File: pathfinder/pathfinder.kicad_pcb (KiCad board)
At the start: 4 copper layers, 30 x 8.1 mm, 66 parts, among them IC1 TESEO-LIV3R, IC2 BMI323, IC3 BMP390, IC4 BGA725L6E6327FTSA1, IC5 ST730M33R, J3 CAS left, J4 CAS right, P2 USB_C_Plug_USB2.0, U1 STM32F042C6Ux, U2 LP2985-1.8, U3 ECMF02-2AMX6, U4 B39162B4327P810

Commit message: Start components layout
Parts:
- removed D6: Green, Diode_SMD:D_0603_1608Metric_Pad1.05x0.95mm_HandSolder
- removed R6: 420, Resistor_SMD:R_0603_1608Metric_Pad0.98x0.95mm_HandSolder
- AC1: footprint sensor_fuser:LGA-12 -> pathfinder:LGA-12
- C1, C10, C11, C12, C13, C14, C15, C16, C17, C18, C19, C2, C20, C21, C22, C23, C24, C25, C26, C27, C28, C3, C4, C5, C6, C7, C8, C9: footprint Capacitor_SMD:C_0603_1608Metric_Pad1.08x0.95mm_HandSolder -> Capacitor_SMD:C_0402_1005Metric_Pad0.74x0.62mm_HandSolder
- D1, D2, D4, D5, D8: footprint Diode_SMD:D_0603_1608Metric_Pad1.05x0.95mm_HandSolder -> Diode_SMD:D_0402_1005Metric_Pad0.77x0.64mm_HandSolder
- R1, R10, R2, R3, R4, R5, R7, R8, R9: footprint Resistor_SMD:R_0603_1608Metric_Pad0.98x0.95mm_HandSolder -> Resistor_SMD:R_0402_1005Metric_Pad0.72x0.64mm_HandSolder
- moved R7 159.8 mm to (131.8, 51.3), turned to -90 degrees
- moved R5 156.8 mm to (130.1, 51.3), turned to -90 degrees
- moved C16 153.0 mm to (146.3, 67.4), turned to -90 degrees
- moved R8 152.7 mm to (136.7, 67.8), turned to 180 degrees
- moved C17 151.3 mm to (141.7, 67.3), turned to -90 degrees
- moved D5 149.3 mm to (131.8, 49.0), turned to -90 degrees
- moved C15 146.9 mm to (143.4, 70.9)
- moved U2 146.3 mm to (144.0, 68.3)
- moved D4 146.3 mm to (130.1, 49.0), turned to -90 degrees
- moved D8 143.5 mm to (136.7, 66.7)
- moved IC5 142.4 mm to (133.8, 68.3)
- moved D7 139.2 mm to (130.9, 64.4), turned to 90 degrees
- moved C11 138.7 mm to (130.9, 66.7), turned to 180 degrees
- moved C10 136.3 mm to (130.9, 67.8), turned to 180 degrees
- moved C9 133.9 mm to (130.9, 68.8), turned to 180 degrees
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
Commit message: Board finished
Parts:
- removed D4: Green, Diode_SMD:D_0402_1005Metric_Pad0.77x0.64mm_HandSolder
- removed P2: USB_C_Plug_USB2.0, Connector_USB:USB_C_Receptacle_G-Switch_GT-USB-7010ASV
- added C29: 100n, Capacitor_SMD:C_0402_1005Metric_Pad0.74x0.62mm_HandSolder, F.Cu at (132.3, 86.9)
- added C30: 100n, Capacitor_SMD:C_0402_1005Metric_Pad0.74x0.62mm_HandSolder, F.Cu at (129.8, 89.1)
- added C31: 23p, Capacitor_SMD:C_0402_1005Metric_Pad0.74x0.62mm_HandSolder, F.Cu at (134.9, 84.1)
- added C32: 23p, Capacitor_SMD:C_0402_1005Metric_Pad0.74x0.62mm_HandSolder, F.Cu at (135.6, 87.8)
- added D6: SZNUP2105L, Package_TO_SOT_SMD:SOT-23, F.Cu at (130.0, 82.6)
- added IC6: TCAN3413DDFR, pathfinder:SOT65P280X110-8N, F.Cu at (130.0, 86.5)
- added J1: USB_C_Receptacle_USB2.0_14P, Connector_USB:USB_C_Receptacle_GCT_USB4105-xx-A_16P_TopMnt_Horizontal, F.Cu at (139.2, 58.3)
- added J2: RF IN, pathfinder:CONUFL001SMDT, F.Cu at (150.2, 101.5)
- added JP1: CAN jumper, Jumper:SolderJumper-2_P1.3mm_Open_RoundedPad1.0x1.5mm, F.Cu at (126.2, 89.3)
- added R11: 3.3k, Resistor_SMD:R_0402_1005Metric_Pad0.72x0.64mm_HandSolder, F.Cu at (148.2, 83.1)
- added R6: 120, Resistor_SMD:R_0402_1005Metric_Pad0.72x0.64mm_HandSolder, F.Cu at (126.2, 87.0)
- added Y1: 16Mhz, Crystal:Crystal_SMD_2016-4Pin_2.0x1.6mm, F.Cu at (135.3, 86.0)
- U1: value STM32F042C6Ux -> STM32G431CBUx
- moved R3 83.2 mm to (150.4, 89.1), turned to 180 degrees
- moved R4 82.7 mm to (150.4, 92.2), turned to 180 degrees
- moved D2 76.6 mm to (150.4, 91.2)
- moved D1 75.2 mm to (150.4, 90.2)
- moved C24 70.8 mm to (128.1, 98.0), turned to 180 degrees
- moved C23 67.4 mm to (142.7, 100.8), turned to 90 degrees
- moved C28 66.2 mm to (150.2, 105.5), turned to -90 degrees
- moved R10 66.1 mm to (142.7, 103.1), turned to -90 degrees
- moved C25 62.3 mm to (128.1, 99.1), turned to 180 degrees
- moved C22 61.5 mm to (128.1, 102.4)
- moved C27 60.9 mm to (146.7, 107.5)
- moved R9 60.8 mm to (128.1, 105.9)
- moved C26 59.6 mm to (142.7, 105.4), turned to 90 degrees
- moved L3 59.3 mm to (148.9, 106.0), turned to 90 degrees
- moved L2 58.2 mm to (127.5, 103.6), turned to 180 degrees
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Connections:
- AC1 pad 1: /Magnetometer/SCL -> /I2C1_SCL
- AC1 pad 11: /Magnetometer/ACC_INT1 -> /ACC2_INT1
- AC1 pad 12: /Magnetometer/ACC_INT2 -> /ACC2_INT2
- AC1 pad 4: /Magnetometer/SDA -> /I2C1_SDA
- AC1 pad 7: /Magnetometer/INT1 -> /MAG_INT1
- C10 pad 1: Net-(D3-K) -> /Power/PWR
- C11 pad 1: Net-(D3-K) -> /Power/PWR
- C15 pad 1: Net-(D3-K) -> /Power/PWR
- C24 pad 1: /GPS/UART_RX -> /UART1_RX
- C25 pad 1: /GPS/UART_TX -> /UART1_TX
- D3 pad 1: Net-(D3-K) -> /Power/PWR
- D7 pad 1: Net-(D3-K) -> /Power/PWR
- H4 pad 1: GND -> unconnected-(H4-Pad1)
- IC1 pad 2: /GPS/UART_RX -> /UART1_RX
- IC1 pad 3: /GPS/UART_TX -> /UART1_TX
- IC2 pad 1: /IMU/MISO -> /SPI1_MISO
- IC2 pad 12: /IMU/CSB -> /SPI1_CS
- IC2 pad 13: /IMU/SCK -> /SPI1_SCK
- IC2 pad 14: /IMU/MOSI -> /SPI1_MOSI
- IC2 pad 4: /IMU/INT1 -> /IMU_INT1
- IC2 pad 9: /IMU/INT2 -> /IMU_INT2
- IC3 pad 2: /Barometer/SCL -> /I2C1_SCL
- IC3 pad 4: /Barometer/SDA -> /I2C1_SDA
- IC3 pad 7: /Barometer/INT -> /BAR_INT1
- IC5 pad 3: Net-(D3-K) -> /Power/PWR
- IC5 pad 5: Net-(D3-K) -> /Power/PWR
- J3 pad 10: GND -> /CAN+
- J3 pad 3: unconnected-(J3-Pin_3-Pad3) -> +3V3
- J3 pad 4: unconnected-(J3-Pin_4-Pad4) -> GND
- J3 pad 5: unconnected-(J3-Pin_5-Pad5) -> /SPI1_MOSI
- J3 pad 6: unconnected-(J3-Pin_6-Pad6) -> /SPI1_MISO
- J3 pad 7: unconnected-(J3-Pin_7-Pad7) -> /SPI1_SCK
- J3 pad 8: unconnected-(J3-Pin_8-Pad8) -> /SPI1_CS
- J3 pad 9: unconnected-(J3-Pin_9-Pad9) -> /CAN-
- J4 pad 10: +3V3 -> /SWD
- J4 pad 3: unconnected-(J4-Pin_3-Pad3) -> /I2C1_SCL
- J4 pad 4: unconnected-(J4-Pin_4-Pad4) -> /I2C1_SDA
- J4 pad 5: unconnected-(J4-Pin_5-Pad5) -> /USART1_RX
- J4 pad 6: unconnected-(J4-Pin_6-Pad6) -> /USART1_TX
- J4 pad 7: unconnected-(J4-Pin_7-Pad7) -> GND
- J4 pad 8: unconnected-(J4-Pin_8-Pad8) -> /NRST
- J4 pad 9: unconnected-(J4-Pin_9-Pad9) -> /CLK
- R1 pad 2: /Barometer/SDA -> /I2C1_SDA
- R2 pad 2: /Barometer/SCL -> /I2C1_SCL
- R5 pad 1: Net-(D4-A) -> Net-(U1-PG10)
- R5 pad 2: Net-(D3-K) -> +3V3
- R7 pad 2: Net-(D3-K) -> /Power/PWR
- U1 pad 10: unconnected-(U1-PA0-Pad10) -> /UART1_TX
- U1 pad 11: unconnected-(U1-PA1-Pad11) -> /UART1_RX
- U1 pad 12: unconnected-(U1-PA2-Pad12) -> /SPI1_CS
- U1 pad 13: unconnected-(U1-PA3-Pad13) -> /SPI1_SCK
- U1 pad 14: unconnected-(U1-PA4-Pad14) -> /SPI1_MISO
- U1 pad 15: unconnected-(U1-PA5-Pad15) -> /SPI1_MOSI
- U1 pad 2: unconnected-(U1-PC13-Pad2) -> /IMU_INT1
- U1 pad 21: unconnected-(U1-PB10-Pad21) -> /MCU_PWR
- U1 pad 22: unconnected-(U1-PB11-Pad22) -> /USART1_TX
- U1 pad 23: GND -> /MCU_PWR
- U1 pad 24: /MCU_PWR -> /USART1_RX
- U1 pad 29: unconnected-(U1-PA8-Pad29) -> /ACC2_INT2
- U1 pad 3: unconnected-(U1-PC14-Pad3) -> /IMU_INT2
- U1 pad 30: unconnected-(U1-PA9-Pad30) -> /ACC2_INT1
- U1 pad 31: unconnected-(U1-PA10-Pad31) -> /DEBUG_LED1
- U1 pad 32: unconnected-(U1-PA11-Pad32) -> /DEBUG_LED0
- U1 pad 33: unconnected-(U1-PA12-Pad33) -> /USB_DM
- U1 pad 34: unconnected-(U1-PA13-Pad34) -> /USB_DP
- U1 pad 35: GND -> /MCU_PWR
- U1 pad 36: /MCU_PWR -> /SWD
- U1 pad 37: unconnected-(U1-PA14-Pad37) -> /CLK
- U1 pad 38: unconnected-(U1-PA15-Pad38) -> /I2C1_SCL
- U1 pad 39: unconnected-(U1-PB3-Pad39) -> /MAG_INT1
- U1 pad 41: unconnected-(U1-PB5-Pad41) -> /SWO
- U1 pad 44: unconnected-(U1-PF11-Pad44) -> /BAR_INT1
- U1 pad 45: unconnected-(U1-PB8-Pad45) -> /I2C1_SDA
- U1 pad 46: unconnected-(U1-PB9-Pad46) -> /FDCAN_RX
- U1 pad 47: GND -> /FDCAN_TX
- U1 pad 5: unconnected-(U1-PF0-Pad5) -> Net-(U1-PF0)
- U1 pad 6: unconnected-(U1-PF1-Pad6) -> Net-(U1-PF1)
- U1 pad 7: unconnected-(U1-NRST-Pad7) -> Net-(U1-PG10)
- U1 pad 8: GND -> unconnected-(U1-PA0-Pad8)
- U1 pad 9: /MCU_PWR -> unconnected-(U1-PA1-Pad9)
- U2 pad 1: Net-(D3-K) -> /Power/PWR
- U2 pad 3: Net-(D3-K) -> /Power/PWR
- U3 pad 5: /USB/D- -> /USB_DM
- U3 pad 6: /USB/D+ -> /USB_DP
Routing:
- net GND: track 0.00 -> 61.3 mm, vias 0 -> 254
- net /SPI1_CS: track 0.00 -> 43.7 mm, vias 0 -> 2
- net /SPI1_MOSI: track 0.00 -> 43.6 mm, vias 0 -> 2
- net /SPI1_SCK: track 0.00 -> 41.3 mm, vias 0 -> 2
- net /SPI1_MISO: track 0.00 -> 41.2 mm, vias 0 -> 2
- net /I2C1_SCL: track 0.00 -> 35.2 mm, vias 0 -> 4
- net /MCU_PWR: track 0.00 -> 33.2 mm, vias 0 -> 6
- net /USB_DP: track 0.00 -> 32.6 mm, vias 0 -> 2
- net /I2C1_SDA: track 0.00 -> 31.1 mm, vias 0 -> 4
- net /USB_DM: track 0.00 -> 30.7 mm
- net +3V3: track 0.00 -> 27.9 mm, vias 0 -> 17
- net /USART1_TX: track 0.00 -> 25.5 mm
- net +5V: track 0.00 -> 23.8 mm, vias 0 -> 2
- net /USART1_RX: track 0.00 -> 22.6 mm
- net /ACC2_INT2: track 0.00 -> 20.9 mm, vias 0 -> 2
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- added copper zone on In1.Cu, net +3V3
- added copper zone on F.Cu, net /Power/PWR
- added copper zone on B.Cu, net GND
- added copper zone on F.Cu, net GND
- added copper zone on F.Cu, net Net-(IC1-VBATT)
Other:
- board size 30 x 8.1 mm -> 30 x 57.8 mm

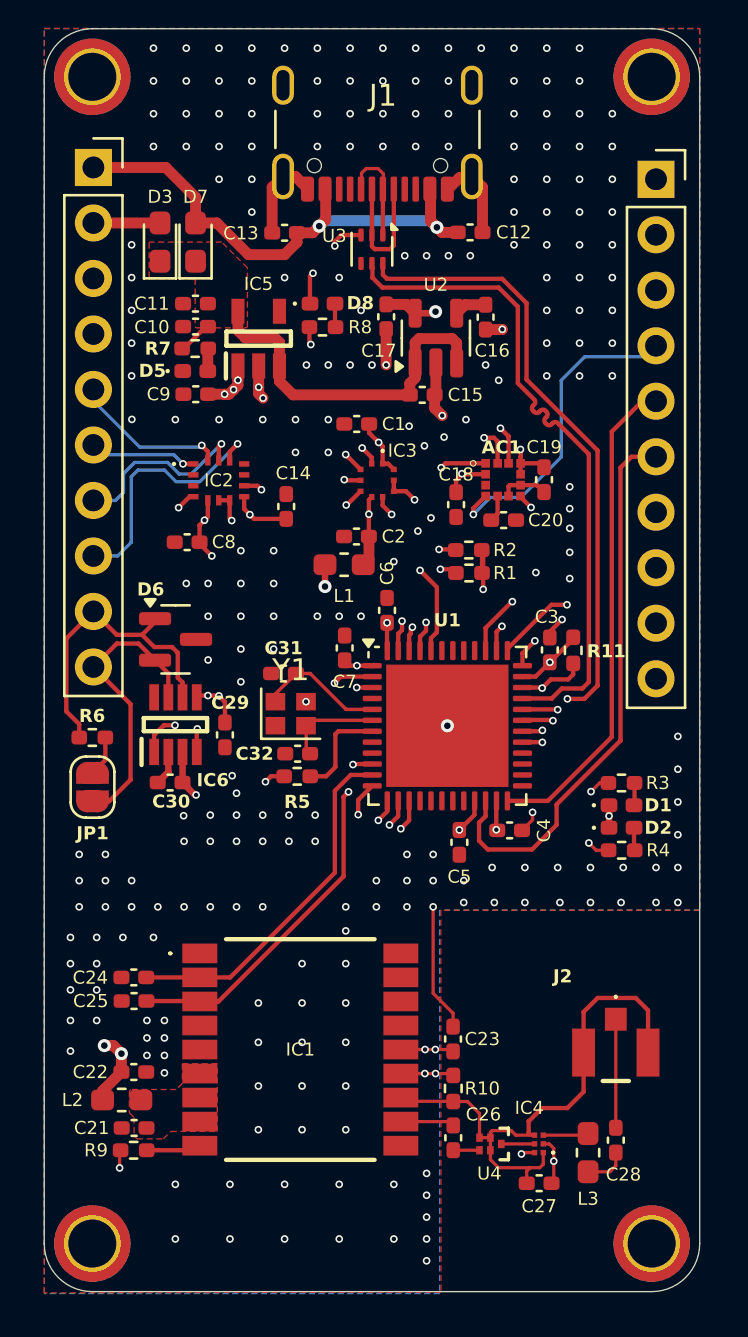
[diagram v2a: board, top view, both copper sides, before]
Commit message: Add optocoupler
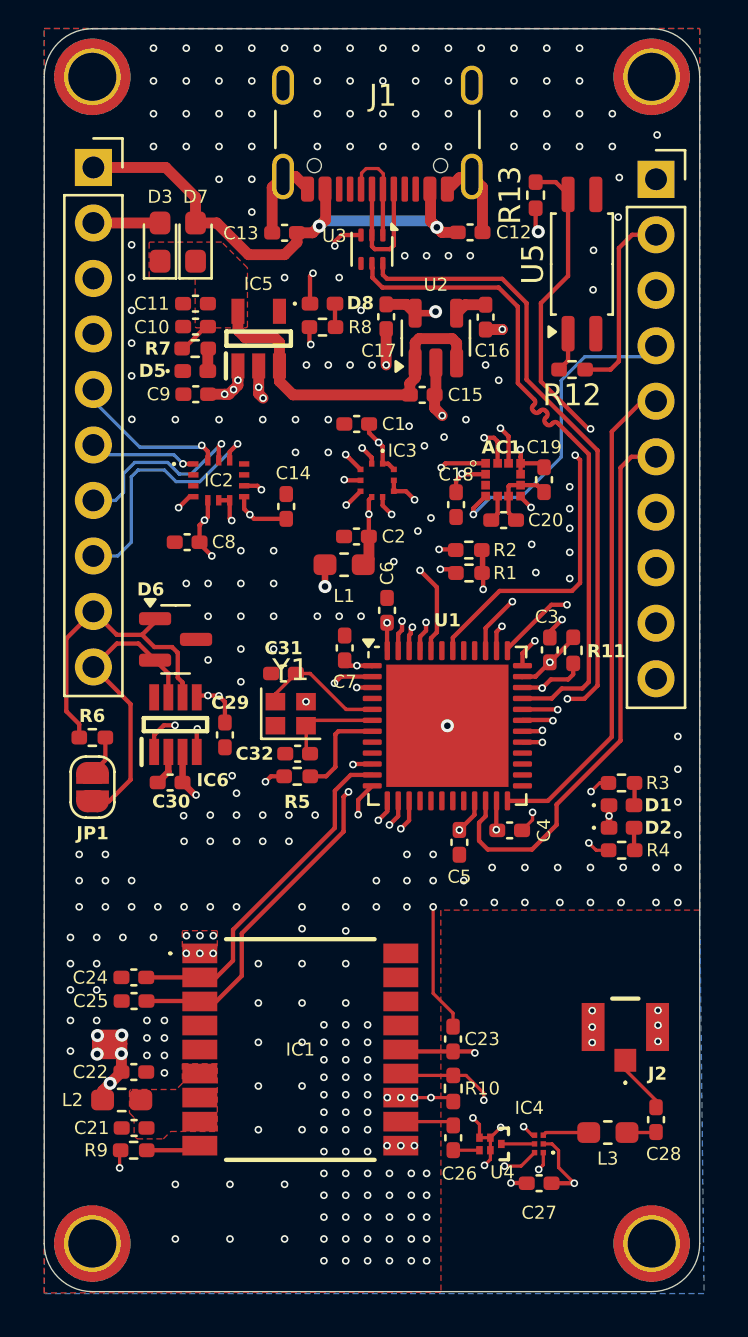
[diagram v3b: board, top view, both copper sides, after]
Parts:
- added R12: 2k, Resistor_SMD:R_0402_1005Metric_Pad0.72x0.64mm_HandSolder, F.Cu at (148.2, 70.2)
- added R13: 2k, Resistor_SMD:R_0402_1005Metric_Pad0.72x0.64mm_HandSolder, F.Cu at (146.5, 62.2)
- added U5: TCMT1102, Package_SO:SOP-4_4.4x2.6mm_P1.27mm, F.Cu at (148.6, 65.4)
- moved C28 2.07 mm to (152.0, 104.5)
- moved L3 1.29 mm to (149.8, 105.1), turned to 180 degrees
- moved J2 1.25 mm to (150.6, 100.3), turned to 0 degrees
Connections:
- J4 pad 1: GND -> /PWM_SRC
- J4 pad 2: unconnected-(J4-Pin_2-Pad2) -> /PWM_IN
- U1 pad 42: unconnected-(U1-PB4-Pad42) -> /PWM_OUT
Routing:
- net /PWM_OUT: track 0.00 -> 28.9 mm, vias 0 -> 2
- net GND: track 61.3 -> 52.0 mm, vias 254 -> 304
- net /PWM_IN: track 0.00 -> 8.84 mm
- net +3V3: track 27.9 -> 33.1 mm, vias 17 -> 21
- net /GPS/VCC_RF: track 14.0 -> 16.6 mm, vias 3 -> 2
- net Net-(J2-In): track 4.97 -> 2.73 mm
- net Net-(R12-Pad2): track 0.00 -> 1.81 mm
- net /I2C1_SCL: track 35.2 -> 34.0 mm
- net /GPS/ANT_OFF: track 10.6 -> 9.66 mm, vias 3 -> 2
- net Net-(C28-Pad2): track 2.12 -> 1.34 mm
- net /PWM_SRC: track 0.00 -> 0.66 mm

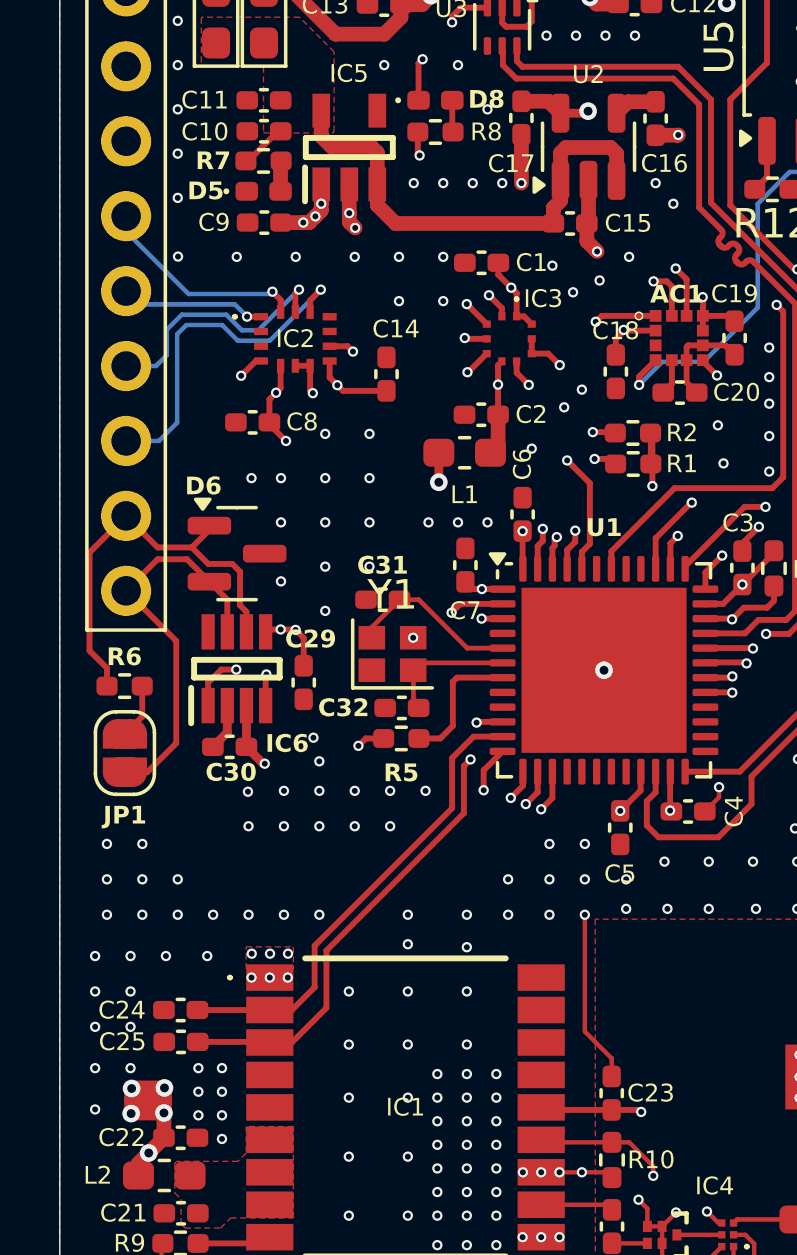
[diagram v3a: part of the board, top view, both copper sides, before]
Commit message: change 1v8 ldo power supply
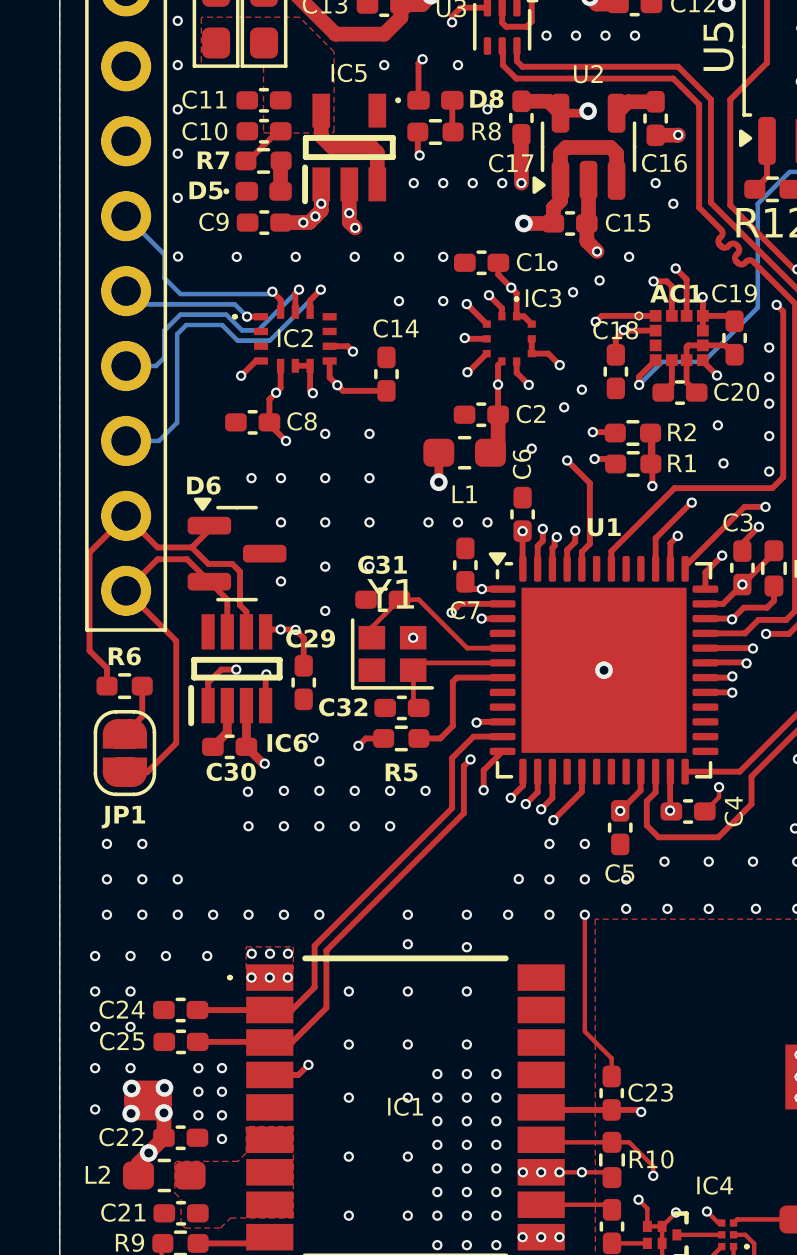
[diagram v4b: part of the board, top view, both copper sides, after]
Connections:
- net /GPS/TIME_PULSE renamed /TIME_PULSE
- C15 pad 1: /Power/PWR -> +3V3
- U2 pad 1: /Power/PWR -> +3V3
- U2 pad 3: /Power/PWR -> +3V3
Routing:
- net /TIME_PULSE: track 0.00 -> 16.0 mm, vias 0 -> 2
- net /Power/PWR: track 18.1 -> 5.68 mm
- net +3V3: track 33.1 -> 39.6 mm, vias 21 -> 22
- net /I2C1_SCL: track 34.0 -> 36.4 mm
